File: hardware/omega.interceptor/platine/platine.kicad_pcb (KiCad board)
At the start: 2 copper layers, 104.1 x 48.3 mm, 10 parts, among them J1 USB_B_Micro, U1 LD1117S33TR_SOT223, U2 Omega2+

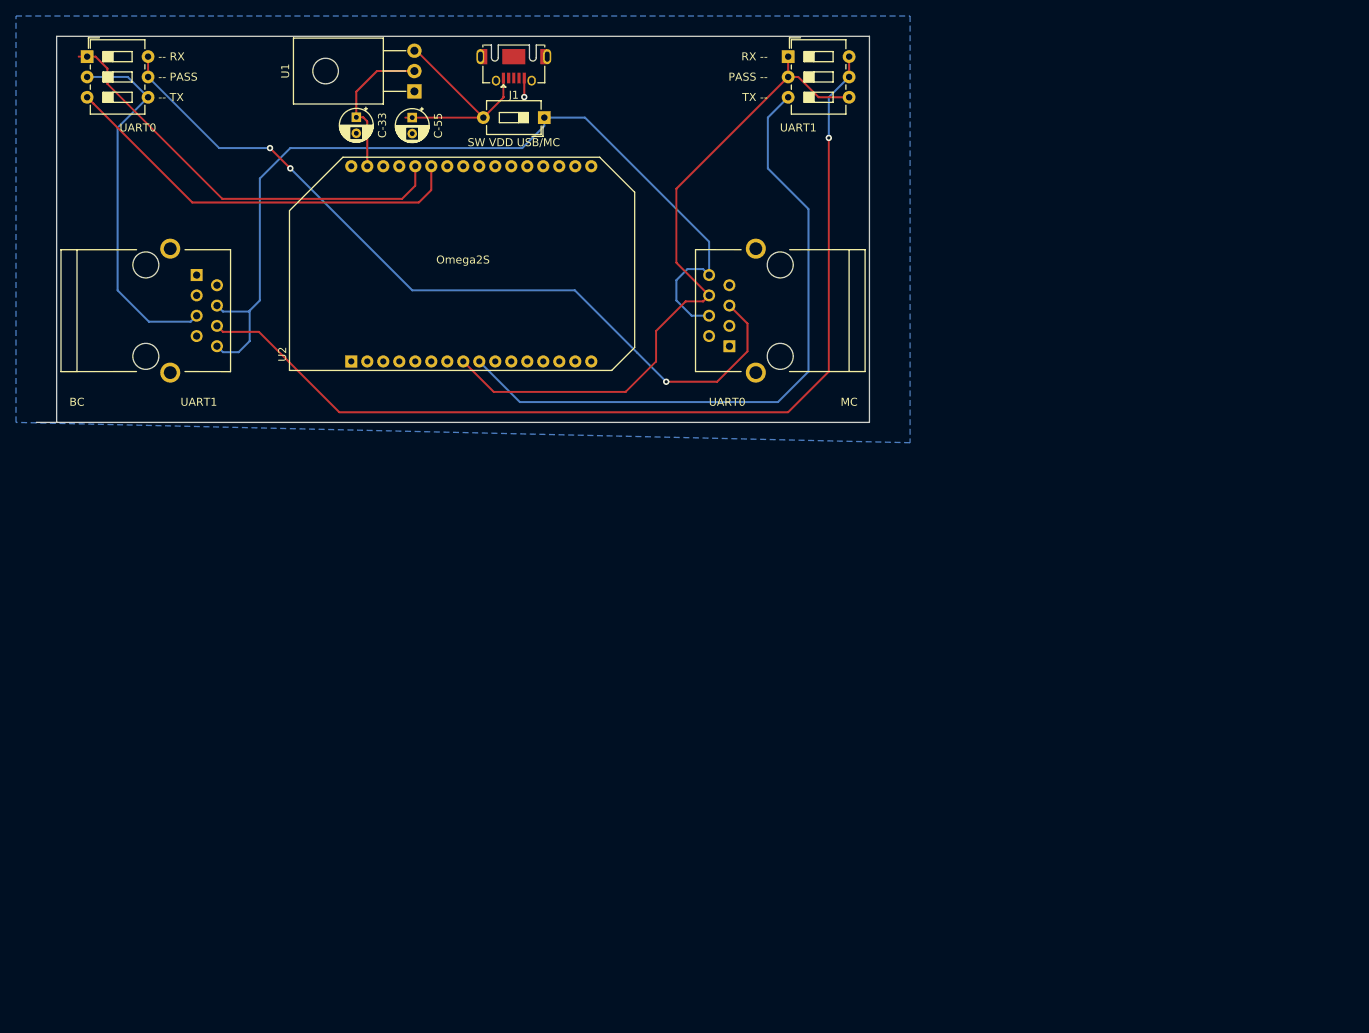
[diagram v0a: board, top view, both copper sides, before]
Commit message: Signifikant changes to interceptor hardware layout * removed usb connector * removed switches for interceptor
made an easy setup to get it manifactured fast and to start testing the protocol
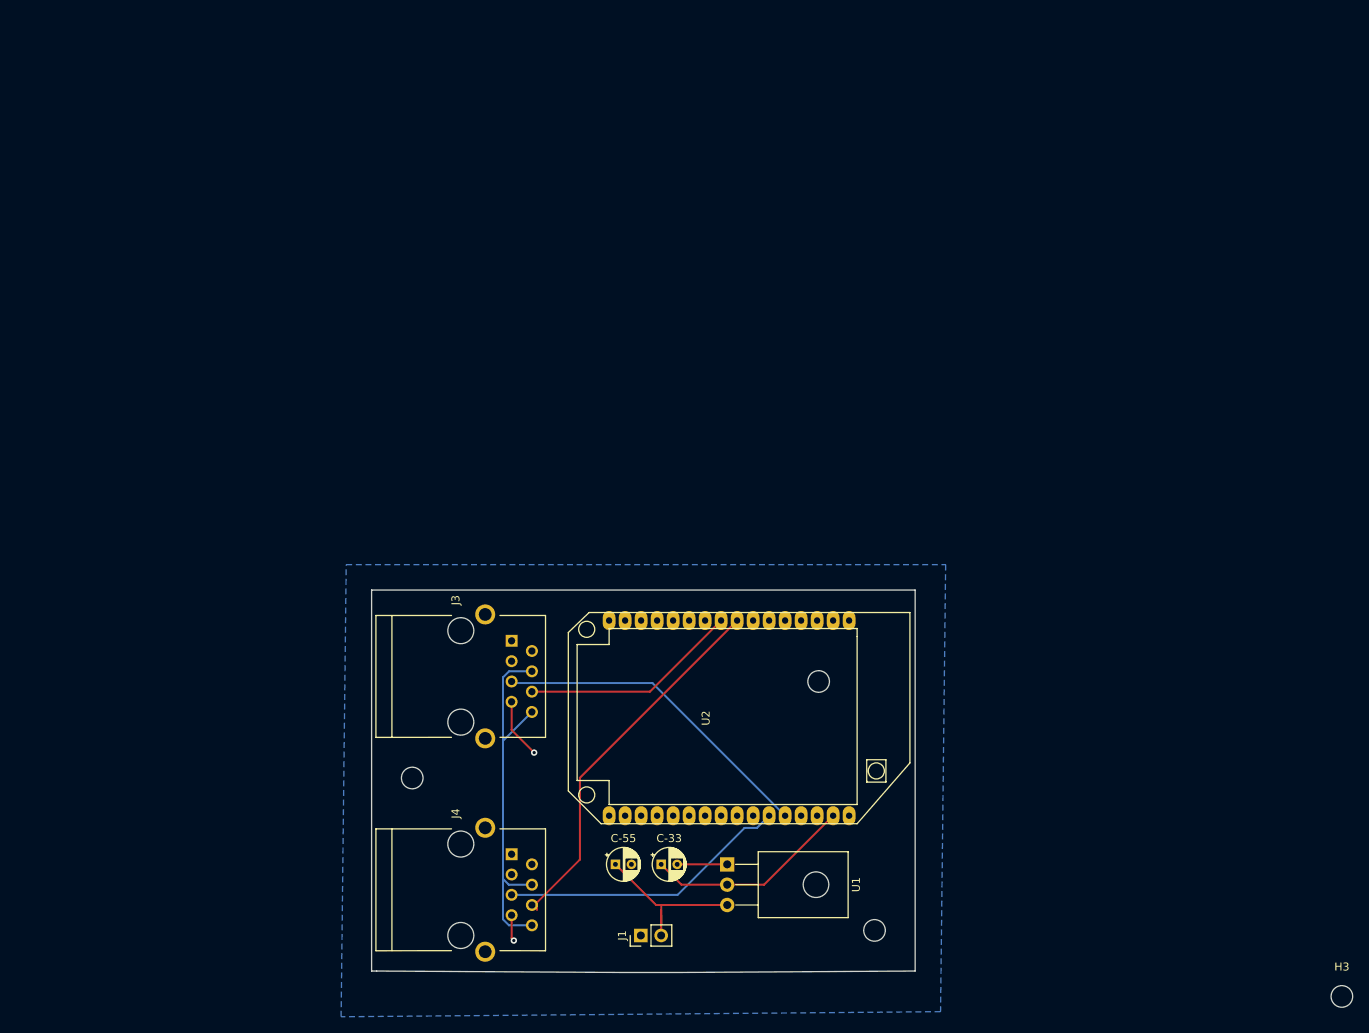
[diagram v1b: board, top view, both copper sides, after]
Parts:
- removed BC, MC: RJ45, Custom-Connectors:MEBP_8-8G
- removed SW VDD USB/MC: SW_DIP_x01, Button_Switch_THT:SW_DIP_SPSTx01_Slide_6.7x4.1mm_W7.62mm_P2.54mm_LowProfile
- removed UART0, UART1: SW_DIP_x03, Button_Switch_THT:SW_DIP_SPSTx03_Slide_6.7x9.18mm_W7.62mm_P2.54mm_LowProfile
- added H1: MountingHole, MountingHole:MountingHole_2.7mm_M2.5, F.Cu at (175.9, 139.7)
- added H2: MountingHole, MountingHole:MountingHole_2.7mm_M2.5, F.Cu at (168.9, 108.6)
- added H3: MountingHole, MountingHole:MountingHole_2.7mm_M2.5, F.Cu at (234.3, 148.0)
- added H4: MountingHole, MountingHole:MountingHole_2.7mm_M2.5, F.Cu at (118.1, 120.7)
- added J3: RJ45, Custom-Connectors:MEBP_8-8G, F.Cu at (115.6, 108.0)
- added J4: RJ45, Custom-Connectors:MEBP_8-8G, F.Cu at (115.6, 134.6)
- J1: value USB_B_Micro -> Conn_01x02; footprint Connector_USB:USB_Micro-AB_Molex_47590-0001 -> Connector_PinHeader_2.54mm:PinHeader_1x02_P2.54mm_Vertical
- U2: footprint Module:Onion_Omega2+ -> Custom-Connectors:ONION_OMEGA2
- moved J1 111.0 mm to (146.7, 140.3), turned to 90 degrees
- moved U1 104.2 mm to (157.5, 131.4), turned to 270 degrees
- moved C-33 100.9 mm to (149.2, 131.4), turned to 0 degrees
- moved C-55 96.7 mm to (143.5, 131.4), turned to 0 degrees
- moved U2 70.2 mm to (172.7, 101.0), turned to 270 degrees
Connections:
- J1 pad 1: Net-(C-55-Pad1) -> Earth
- J1 pad 2: Net-(J1-Pad2) -> Net-(C-55-Pad1)
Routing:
- net Net-(J4-Pad6) (its old number): track 123.5 -> 0.00 mm, vias 1 -> 0
- net Net-(J3-Pad5) (its old number): track 101.5 -> 0.00 mm, vias 3 -> 0
- net /WAKE: track 113.2 -> 52.7 mm
- net Net-(J3-Pad6): track 82.3 -> 27.3 mm
- net Net-(J4-Pad5) (its old number): track 46.2 -> 0.00 mm
- net Net-(J4-Pad6): track 85.5 -> 46.6 mm
- net Net-(J4-Pad5): track 52.1 -> 36.3 mm
- net Earth: track 2.38 -> 17.1 mm, vias 1 -> 2
- net Net-(J3-Pad5): track 53.7 -> 41.1 mm
- net /3.3V: track 18.8 -> 26.1 mm
- net Net-(C-55-Pad1): track 27.8 -> 22.9 mm
- net Net-(J1-Pad6): track 1.10 -> 0.00 mm
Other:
- board size 104.1 x 48.3 mm -> 67.9 x 47.8 mm
- rule pad_to_mask_clearance: 0.051 -> 0
- board text removed: "-- PASS"
- board text removed: "-- RX"
- board text removed: "-- TX"
- board text removed: "Omega2S"
- board text removed: "PASS --"
- board text removed: "RX --"
- board text removed: "TX --"
- board text removed: "UART0"
- board text removed: "UART1"
